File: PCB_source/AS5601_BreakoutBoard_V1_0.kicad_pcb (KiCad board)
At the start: 2 copper layers, 20 x 13.5 mm, 20 parts, among them P1 CONN_01X07, P2 MountHole_M3, P3 MountHole_M3, U1 AS5601

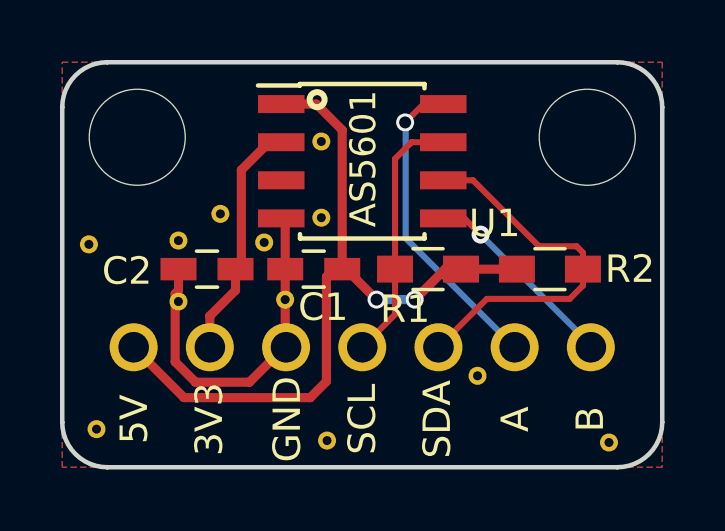
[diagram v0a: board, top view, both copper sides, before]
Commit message: add step and refactoring
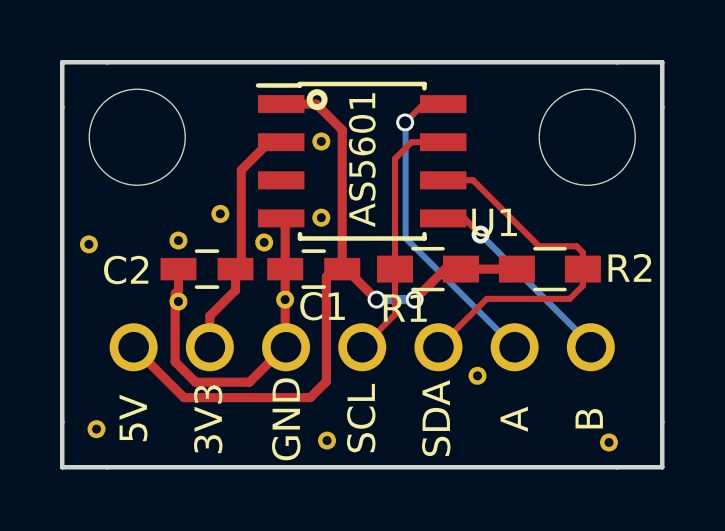
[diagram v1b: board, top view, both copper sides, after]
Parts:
- C1, C2: footprint Capacitors_SMD:C_0603_HandSoldering -> footprints:C_0603_HandSoldering
- P1: footprint user:USER_SIL-7 -> footprints:USER_SIL-7
- R1, R2: footprint Resistors_SMD:R_0603_HandSoldering -> footprints:R_0603_HandSoldering
- U1: footprint Housings_SOIC:SOIC-8_3.9x4.9mm_Pitch1.27mm -> footprints:SOIC-8_3.9x4.9mm_Pitch1.27mm
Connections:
- P2 pad 1: (no net) -> Net-(P2-Pad1)
- P3 pad 1: (no net) -> Net-(P3-Pad1)
- U1 pad 3: (no net) -> Net-(U1-Pad3)
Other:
- outline, holes or cut-outs redrawn
- rule pad_to_mask_clearance: 0.2 -> 0

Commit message: kicad v6
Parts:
- moved 11 110.6 mm to (18.2, 12.7)
- moved 12 110.6 mm to (0.89, 6.07)
- moved 21 110.6 mm to (8.64, 5.18)
- moved 22 110.6 mm to (6.73, 6.01)
- moved 31 110.6 mm to (5.27, 5.05)
- moved 32 110.6 mm to (3.87, 5.94)
- moved 41 110.6 mm to (8.83, 12.6)
- moved 41 110.6 mm to (13.8, 10.5)
- moved 42 110.6 mm to (3.87, 7.98)
- moved 51 110.6 mm to (8.64, 2.64)
- moved 52 110.6 mm to (7.43, 7.91)
- moved ? 110.6 mm to (1.14, 12.2)
- moved C1 110.6 mm to (8.38, 6.90)
- moved C2 110.6 mm to (4.83, 6.90)
- moved P1 110.6 mm to (10.0, 9.50)
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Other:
- net class Default removed
- net class Power removed
- net class Power2 removed
